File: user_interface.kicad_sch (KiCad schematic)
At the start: 0 parts

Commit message: 1.3.1 Schematic design sheet #4: User interface
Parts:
- added J4: Conn_01x04_Pin, symbol Connector:Conn_01x04_Pin
- added J5: Conn_01x05_Pin, symbol Connector:Conn_01x05_Pin
- added Q2, Q3: BC817, Package_TO_SOT_SMD:SOT-23, symbol Transistor_BJT:BC817
- added S1, S2: USLPT2819DT2TR, USLPT2819DT2TR:SW_USLPT2819DT2TR, symbol USLPT2819DT2TR:USLPT2819DT2TR
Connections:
- new net +3.3V: J4.1 (Pin_1), J5.1 (Pin_1)
- new net GND: J4.4 (Pin_4), J5.5 (Pin_5)
- new net GPIO18: J5.3 (Pin_3)
- new net GPIO19: J5.4 (Pin_4)
- new net GPIO8: J5.2 (Pin_2)
- new net SCL: J4.3 (Pin_3)
- new net SDA: J4.2 (Pin_2)
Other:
- note added: "Breakout for remaining pins"
- note added: "OLED display connector (I2C)"

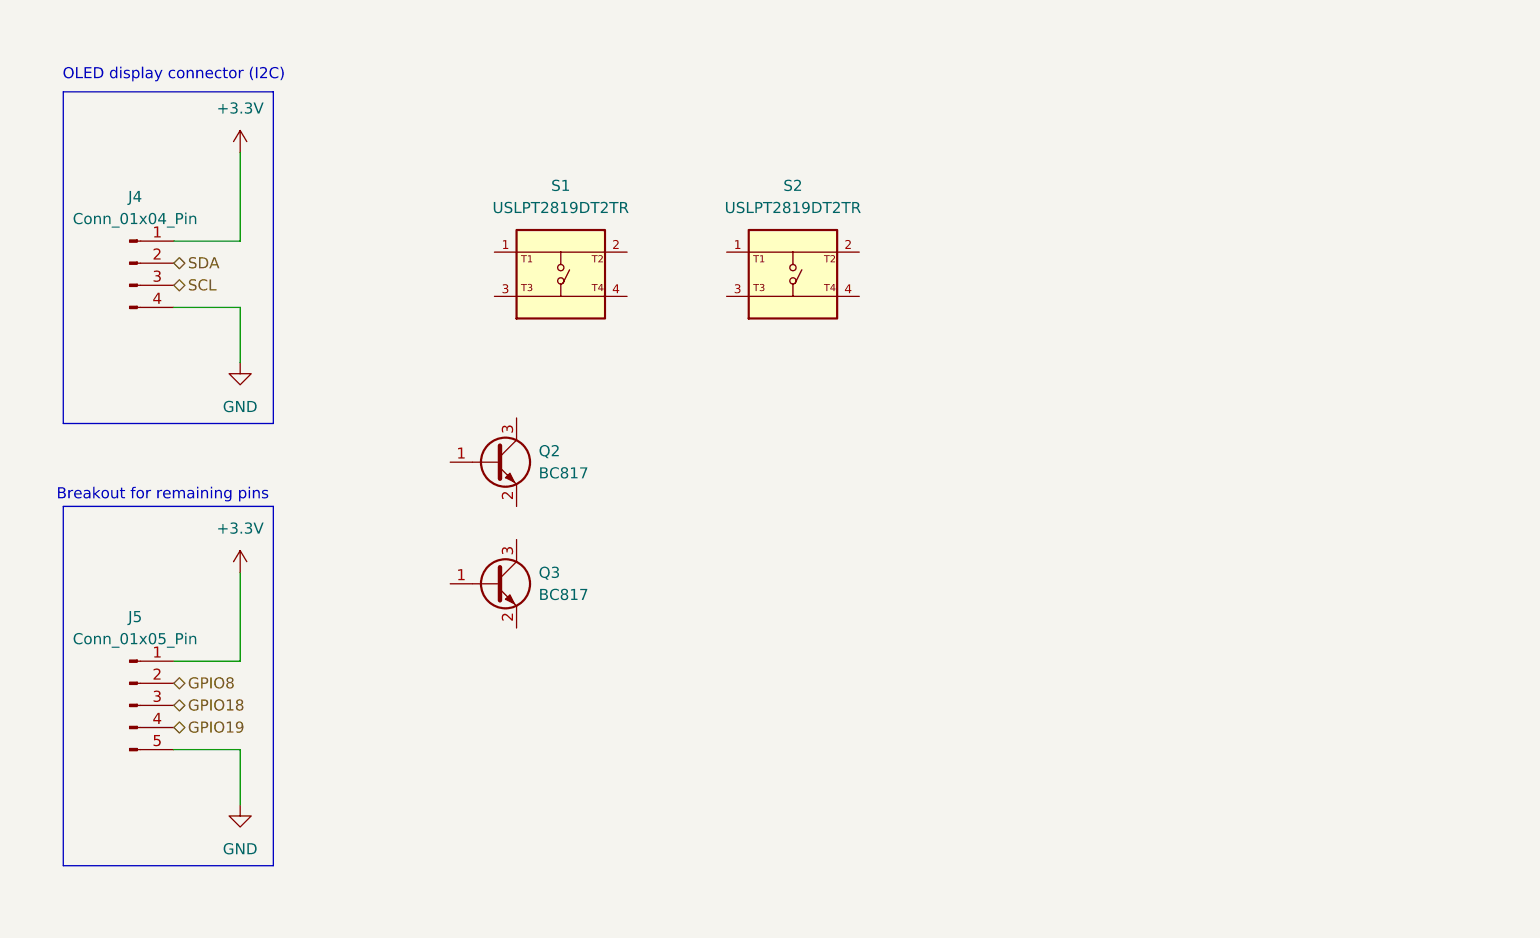
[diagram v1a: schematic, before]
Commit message: 1.3.2 Wiring of the EN and BOOT buttons
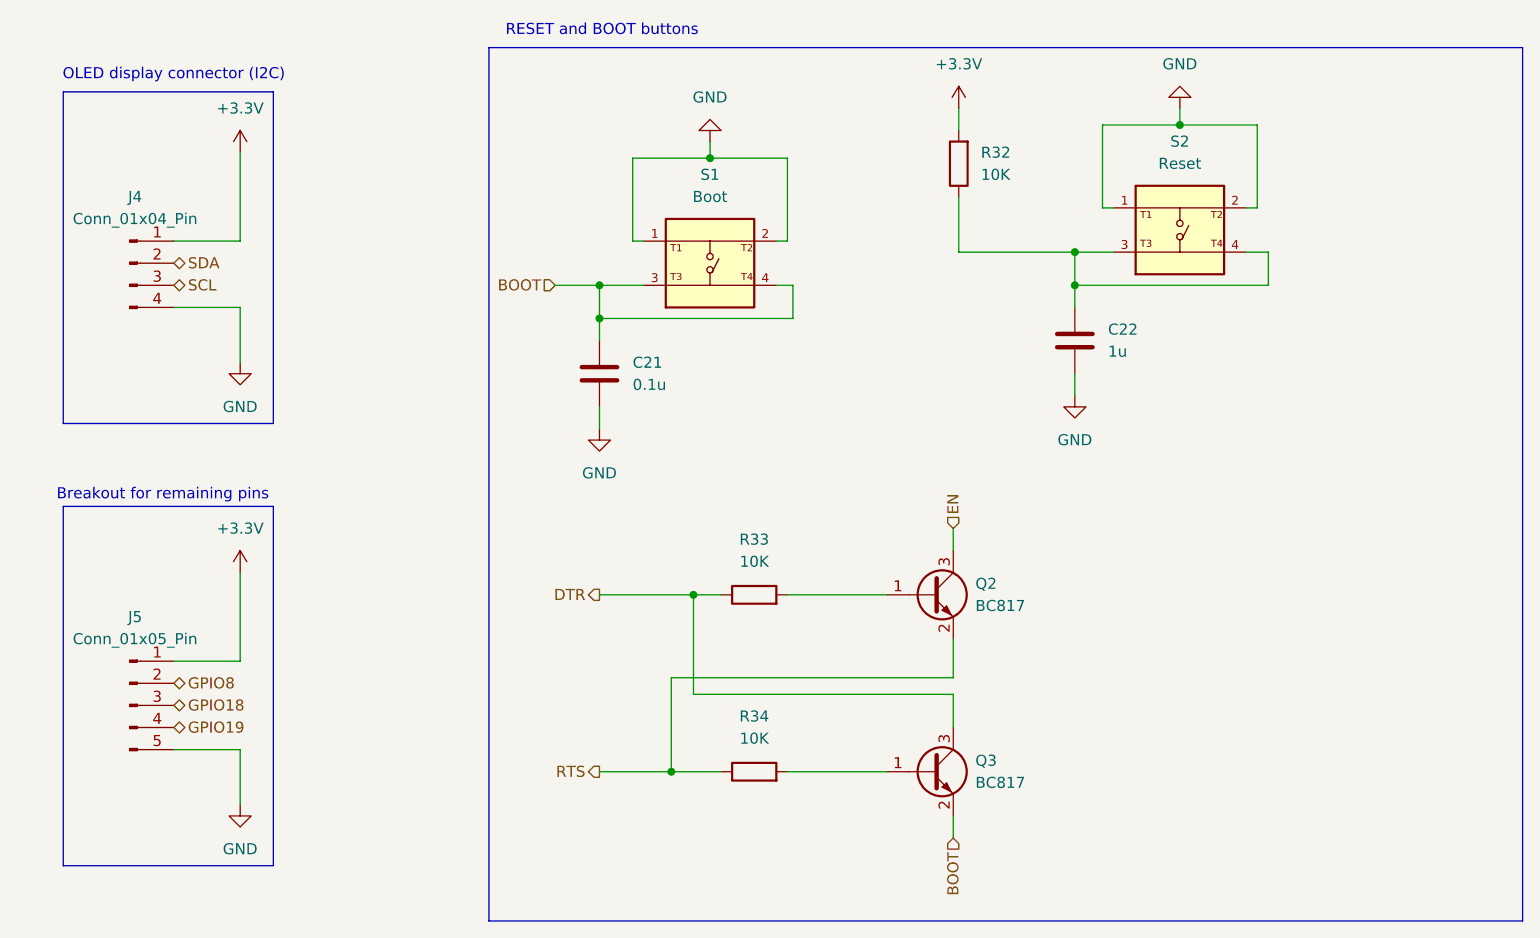
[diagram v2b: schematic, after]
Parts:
- added C21: 0.1u, symbol Device:C
- added C22: 1u, symbol Device:C
- added R32, R33, R34: 10K, symbol Device:R
- S1: value USLPT2819DT2TR -> Boot
- S2: value USLPT2819DT2TR -> Reset
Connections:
- net +3.3V: now also R32.2
- net GND: now also S1.1, S1.2, S2.1, S2.2, C21.2, C22.2
- net BOOT: now reaches S1.3
- net BOOT: now also Q3.2 (E), S1.4, C21.1
- net at Q3.1 (B): now also R34.2
- net DTR: now reaches Q3.3 (C)
- net DTR: now also R33.1
- net at S2.3: now also S2.4, C22.1, R32.1
- net at Q2.1 (B): now also R33.2
- net RTS: now reaches Q2.2 (E)
- net RTS: now also R34.1
- net EN: now reaches Q2.3 (C)
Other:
- note added: "RESET and BOOT buttons"
- moved on the sheet: Q2, Q3, S1, S2

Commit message: 1.3.3 Symbol and footprint associations
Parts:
- C21, C22: footprint (none) -> Capacitor_SMD:C_0805_2012Metric
- J4: footprint (none) -> Connector_PinHeader_2.54mm:PinHeader_1x04_P2.54mm_Vertical
- J5: footprint (none) -> Connector_PinHeader_2.54mm:PinHeader_1x05_P2.54mm_Vertical
- R32, R33, R34: footprint (none) -> Resistor_SMD:R_0805_2012Metric
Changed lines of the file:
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@@
 			)
 		)
-		(property "Footprint" ""
+		(property "Footprint" "Resistor_SMD:R_0805_2012Metric"
 			(at 126.365 126.238 90)
 			(effects
@@
 			)
 		)
-		(property "Footprint" ""
+		(property "Footprint" "Capacitor_SMD:C_0805_2012Metric"
 			(at 164.1602 78.74 0)
 			(effects
@@
 			)
 		)
-		(property "Footprint" ""
+		(property "Footprint" "Resistor_SMD:R_0805_2012Metric"
 			(at 126.365 105.918 90)
 			(effects
@@
 			)
 		)
-		(property "Footprint" ""
+		(property "Footprint" "Capacitor_SMD:C_0805_2012Metric"
 			(at 109.5502 82.55 0)
 			(effects
@@
 			)
 		)
-		(property "Footprint" ""
+		(property "Footprint" "Resistor_SMD:R_0805_2012Metric"
 			(at 151.638 54.61 90)
 			(effects
@@
 			)
 		)
-		(property "Footprint" ""
+		(property "Footprint" "Connector_PinHeader_2.54mm:PinHeader_1x04_P2.54mm_Vertical"
 			(at 54.61 66.04 0)
 			(effects
@@
 			)
 		)
-		(property "Footprint" ""
+		(property "Footprint" "Connector_PinHeader_2.54mm:PinHeader_1x05_P2.54mm_Vertical"
 			(at 54.61 116.84 0)
 			(effects

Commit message: 1.3.9 Bring remaining components to the layout editor
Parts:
- S1, S2: footprint USLPT2819DT2TR:SW_USLPT2819DT2TR -> ESP32_demo_project:USLPT2819DT2TR
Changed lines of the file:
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@@
 			)
 		)
-		(property "Footprint" "USLPT2819DT2TR:SW_USLPT2819DT2TR"
+		(property "Footprint" "ESP32_demo_project:USLPT2819DT2TR"
 			(at 121.285 66.04 0)
 			(effects
@@
 			)
 		)
-		(property "Footprint" "USLPT2819DT2TR:SW_USLPT2819DT2TR"
+		(property "Footprint" "ESP32_demo_project:USLPT2819DT2TR"
 			(at 175.26 62.23 0)
 			(effects
